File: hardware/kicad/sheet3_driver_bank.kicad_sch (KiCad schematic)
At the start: 32 parts, among them U101 TC4427ACOA, U102 TC4427ACOA, U103 TC4427ACOA, U104 TC4427ACOA, U105 TC4427ACOA, U106 TC4427ACOA, U107 TC4427ACOA, U108 TC4427ACOA, U109 TC4427ACOA, U110 TC4427ACOA, U111 TC4427ACOA, U112 TC4427ACOA, U113 TC4427ACOA, U114 TC4427ACOA, U115 TC4427ACOA, U116 TC4427ACOA, U117 TC4427ACOA, U118 TC4427ACOA, U119 TC4427ACOA, U120 TC4427ACOA, U121 TC4427ACOA, U122 TC4427ACOA, U123 TC4427ACOA, U124 TC4427ACOA, U125 TC4427ACOA, U126 TC4427ACOA, U127 TC4427ACOA, U128 TC4427ACOA, U129 TC4427ACOA, U130 TC4427ACOA, U131 TC4427ACOA, U132 TC4427ACOA

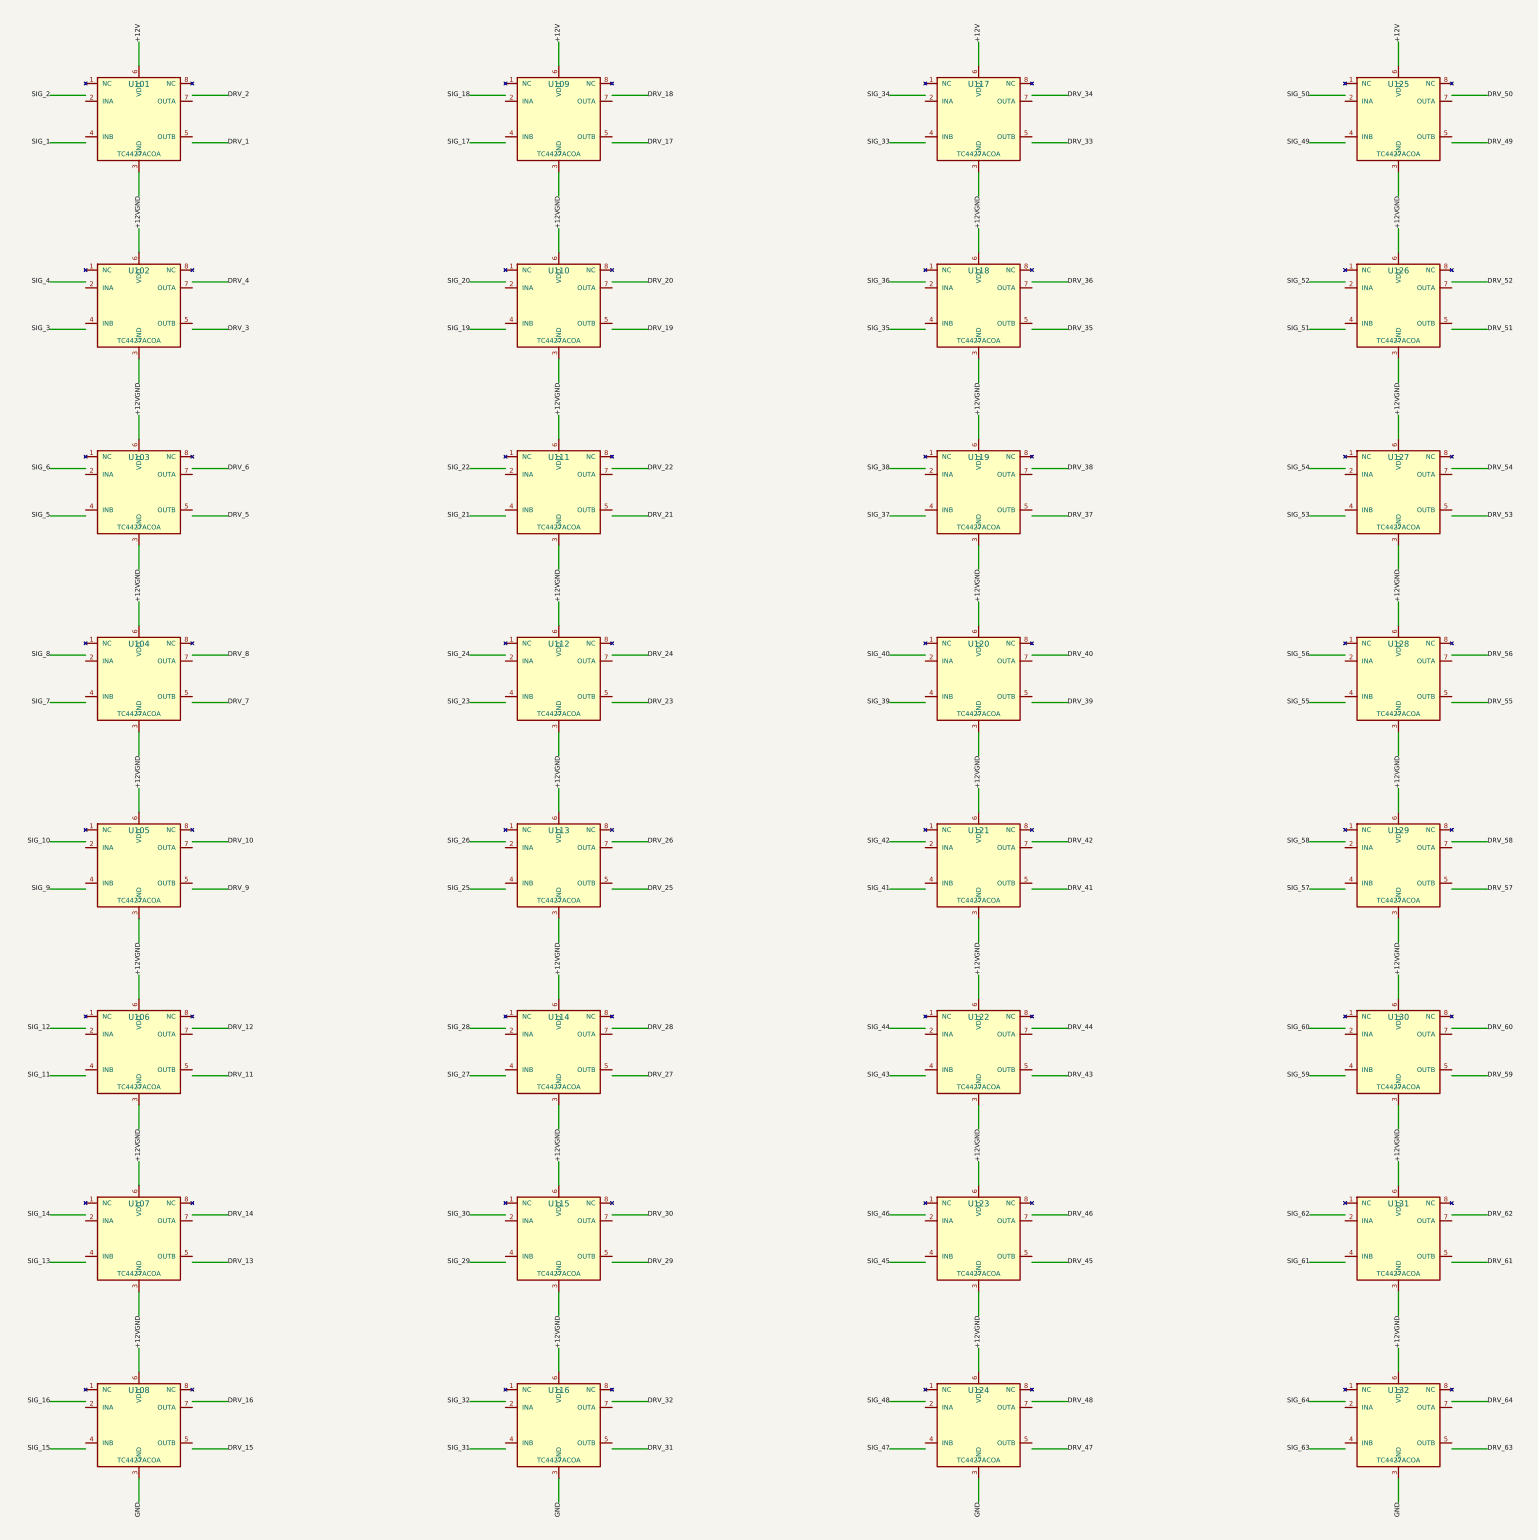
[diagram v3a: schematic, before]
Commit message: Auto-route 392 copper tracks for 64-channel HPVE phased array PCB
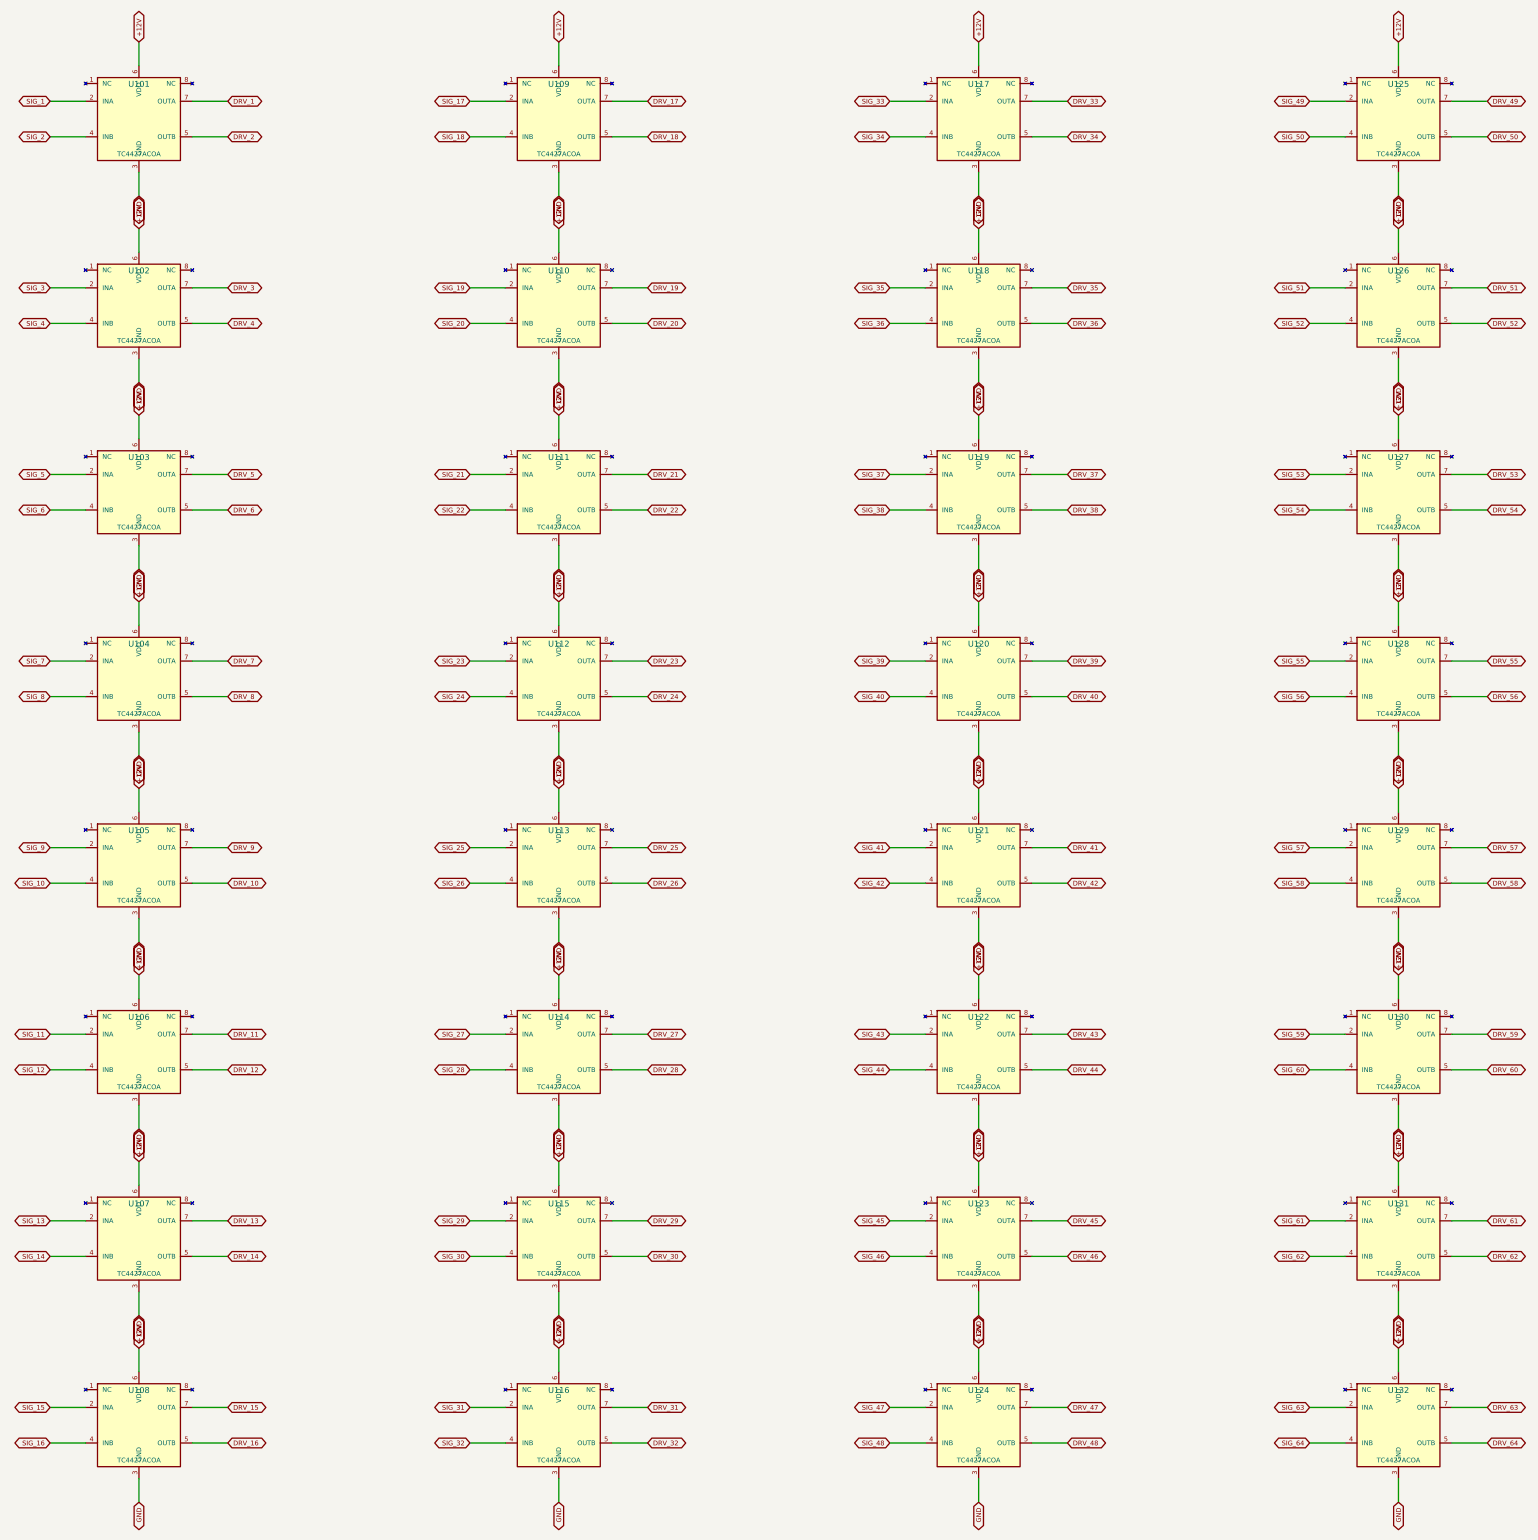
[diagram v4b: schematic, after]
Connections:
- net DRV_1: now also U101.7 (OUTA)
- net DRV_10: now also U105.5 (OUTB)
- net DRV_11: now also U106.7 (OUTA)
- net DRV_12: now also U106.5 (OUTB)
- net DRV_13: now also U107.7 (OUTA)
- net DRV_14: now also U107.5 (OUTB)
- net DRV_15: now also U108.7 (OUTA)
- net DRV_16: now also U108.5 (OUTB)
- net DRV_17: now also U109.7 (OUTA)
- net DRV_18: now also U109.5 (OUTB)
- net DRV_19: now also U110.7 (OUTA)
- net DRV_2: now also U101.5 (OUTB)
- net DRV_20: now also U110.5 (OUTB)
- net DRV_21: now also U111.7 (OUTA)
- net DRV_22: now also U111.5 (OUTB)
- net DRV_23: now also U112.7 (OUTA)
- net DRV_24: now also U112.5 (OUTB)
- net DRV_25: now also U113.7 (OUTA)
- net DRV_26: now also U113.5 (OUTB)
- net DRV_27: now also U114.7 (OUTA)
- net DRV_28: now also U114.5 (OUTB)
- net DRV_29: now also U115.7 (OUTA)
- net DRV_3: now also U102.7 (OUTA)
- net DRV_30: now also U115.5 (OUTB)
- net DRV_31: now also U116.7 (OUTA)
- net DRV_32: now also U116.5 (OUTB)
- net DRV_33: now also U117.7 (OUTA)
- net DRV_34: now also U117.5 (OUTB)
- net DRV_35: now also U118.7 (OUTA)
- net DRV_36: now also U118.5 (OUTB)
- net DRV_37: now also U119.7 (OUTA)
- net DRV_38: now also U119.5 (OUTB)
- net DRV_39: now also U120.7 (OUTA)
- net DRV_4: now also U102.5 (OUTB)
- net DRV_40: now also U120.5 (OUTB)
- net DRV_41: now also U121.7 (OUTA)
- net DRV_42: now also U121.5 (OUTB)
- net DRV_43: now also U122.7 (OUTA)
- net DRV_44: now also U122.5 (OUTB)
- net DRV_45: now also U123.7 (OUTA)
- net DRV_46: now also U123.5 (OUTB)
- net DRV_47: now also U124.7 (OUTA)
- net DRV_48: now also U124.5 (OUTB)
- net DRV_49: now also U125.7 (OUTA)
- net DRV_5: now also U103.7 (OUTA)
- net DRV_50: now also U125.5 (OUTB)
- net DRV_51: now also U126.7 (OUTA)
- net DRV_52: now also U126.5 (OUTB)
- net DRV_53: now also U127.7 (OUTA)
- net DRV_54: now also U127.5 (OUTB)
- net DRV_55: now also U128.7 (OUTA)
- net DRV_56: now also U128.5 (OUTB)
- net DRV_57: now also U129.7 (OUTA)
- net DRV_58: now also U129.5 (OUTB)
- net DRV_59: now also U130.7 (OUTA)
- net DRV_6: now also U103.5 (OUTB)
- net DRV_60: now also U130.5 (OUTB)
- net DRV_61: now also U131.7 (OUTA)
- net DRV_62: now also U131.5 (OUTB)
- net DRV_63: now also U132.7 (OUTA)
- net DRV_64: now also U132.5 (OUTB)
- net DRV_7: now also U104.7 (OUTA)
- net DRV_8: now also U104.5 (OUTB)
- net DRV_9: now also U105.7 (OUTA)
- net SIG_1: now also U101.2 (INA)
- net SIG_10: now also U105.4 (INB)
- net SIG_11: now also U106.2 (INA)
- net SIG_12: now also U106.4 (INB)
- net SIG_13: now also U107.2 (INA)
- net SIG_14: now also U107.4 (INB)
- net SIG_15: now also U108.2 (INA)
- net SIG_16: now also U108.4 (INB)
- net SIG_17: now also U109.2 (INA)
- net SIG_18: now also U109.4 (INB)
- net SIG_19: now also U110.2 (INA)
- net SIG_2: now also U101.4 (INB)
- net SIG_20: now also U110.4 (INB)
- net SIG_21: now also U111.2 (INA)
- net SIG_22: now also U111.4 (INB)
- net SIG_23: now also U112.2 (INA)
- net SIG_24: now also U112.4 (INB)
- net SIG_25: now also U113.2 (INA)
- net SIG_26: now also U113.4 (INB)
- net SIG_27: now also U114.2 (INA)
- net SIG_28: now also U114.4 (INB)
- net SIG_29: now also U115.2 (INA)
- net SIG_3: now also U102.2 (INA)
- net SIG_30: now also U115.4 (INB)
- net SIG_31: now also U116.2 (INA)
- net SIG_32: now also U116.4 (INB)
- net SIG_33: now also U117.2 (INA)
- net SIG_34: now also U117.4 (INB)
- net SIG_35: now also U118.2 (INA)
- net SIG_36: now also U118.4 (INB)
- net SIG_37: now also U119.2 (INA)
- net SIG_38: now also U119.4 (INB)
- net SIG_39: now also U120.2 (INA)
- net SIG_4: now also U102.4 (INB)
- net SIG_40: now also U120.4 (INB)
- net SIG_41: now also U121.2 (INA)
- net SIG_42: now also U121.4 (INB)
- net SIG_43: now also U122.2 (INA)
- net SIG_44: now also U122.4 (INB)
- net SIG_45: now also U123.2 (INA)
- net SIG_46: now also U123.4 (INB)
- net SIG_47: now also U124.2 (INA)
- net SIG_48: now also U124.4 (INB)
- net SIG_49: now also U125.2 (INA)
- net SIG_5: now also U103.2 (INA)
- net SIG_50: now also U125.4 (INB)
- net SIG_51: now also U126.2 (INA)
- net SIG_52: now also U126.4 (INB)
- net SIG_53: now also U127.2 (INA)
- net SIG_54: now also U127.4 (INB)
- net SIG_55: now also U128.2 (INA)
- net SIG_56: now also U128.4 (INB)
- net SIG_57: now also U129.2 (INA)
- net SIG_58: now also U129.4 (INB)
- net SIG_59: now also U130.2 (INA)
- net SIG_6: now also U103.4 (INB)
- net SIG_60: now also U130.4 (INB)
- net SIG_61: now also U131.2 (INA)
- net SIG_62: now also U131.4 (INB)
- net SIG_63: now also U132.2 (INA)
- net SIG_64: now also U132.4 (INB)
- net SIG_7: now also U104.2 (INA)
- net SIG_8: now also U104.4 (INB)
- net SIG_9: now also U105.2 (INA)
